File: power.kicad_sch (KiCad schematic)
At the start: 7 parts, among them J1 USB_C_Receptacle, U1 INA226, U2 AMS1117-3.3, U3 ATmega328P-A

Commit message: Getting there
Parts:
- added C3, C4: 22 pF, symbol Device:C
- added C5, C6: 1µF, symbol Device:C
- added R1, R2: 4.7kΩ, symbol Device:R
- added R3, R4: 5.1kΩ, symbol Device:R
- added Y1: Crystal, symbol Device:Crystal
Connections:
- net 3V3: now also C2.1, DS1.28 (VCC), U1.6 (VS), U1.8 (Vbus), U2.2 (VO), C6.2, R1.2, R2.1; no longer C2.2, DS1.9 (VDD)
- net GND: now also C2.2, C3.2, C4.2, C5.2, C6.1, R3.2, R4.2; no longer J1.S1 (SHIELD)
- net OLED_RESET: now reaches DS1.14 (~{RES})
- net OLED_RESET: now also U3.12 (PB0)
- net D/C: now reaches DS1.15 (D/~{C})
- net D/C: now also U3.13 (PB1)
- net R/W: now reaches DS1.16 (R/~{W})
- net R/W: now also U3.14 (PB2)
- net E/RD: now reaches DS1.17 (E/~{RD})
- net E/RD: now also U3.23 (PC0)
- net D0: now reaches DS1.18 (D0)
- net D0: now also U3.30 (PD0)
- net D1: now reaches DS1.19 (D1)
- net D1: now also U3.31 (PD1)
- net D2: now reaches DS1.20 (D2)
- net D2: now also U3.32 (PD2)
- net D3: now reaches DS1.21 (D3)
- net D3: now also U3.1 (PD3)
- net D4: now reaches DS1.22 (D4)
- net D4: now also U3.2 (PD4)
- net D5: now reaches DS1.23 (D5)
- net D5: now also U3.9 (PD5)
- net D6: now reaches DS1.24 (D6)
- net D6: now also U3.10 (PD6)
- net D7: now reaches DS1.25 (D7)
- net D7: now also U3.11 (PD7)
- net MOSI: now reaches U3.15 (PB3)
- net MISO: now reaches U3.16 (PB4)
- net SCK: now reaches U3.17 (PB5)
- net SDA: now reaches U3.27 (PC4)
- net SDA: now also U1.4 (SDA), R1.1
- net SCL: now reaches U3.28 (PC5)
- net SCL: now also U1.5 (SCL), R2.2
- net RESET: now reaches U3.29 (~{RESET}/PC6)
- net at U3.7 (XTAL1/PB6): now also C4.1, Y1.2
- net at U3.8 (XTAL2/PB7): now also C3.1, Y1.1
- net VBUS: now reaches C1.2, U2.3 (VI)
- net VBUS: now also J1.A4 (VBUS), J1.A9 (VBUS), J1.B4 (VBUS), J1.B9 (VBUS), U1.10 (Vin+)
- net at J1.A5 (CC1): now also R3.1
- net at J1.B5 (CC2): now also R4.1
- net INPUT_PW: now reaches U1.9 (Vin-)
- new net: C5.1, J1.S1 (SHIELD)
- no-connect marks 0 -> 5
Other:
- moved on the sheet: C2

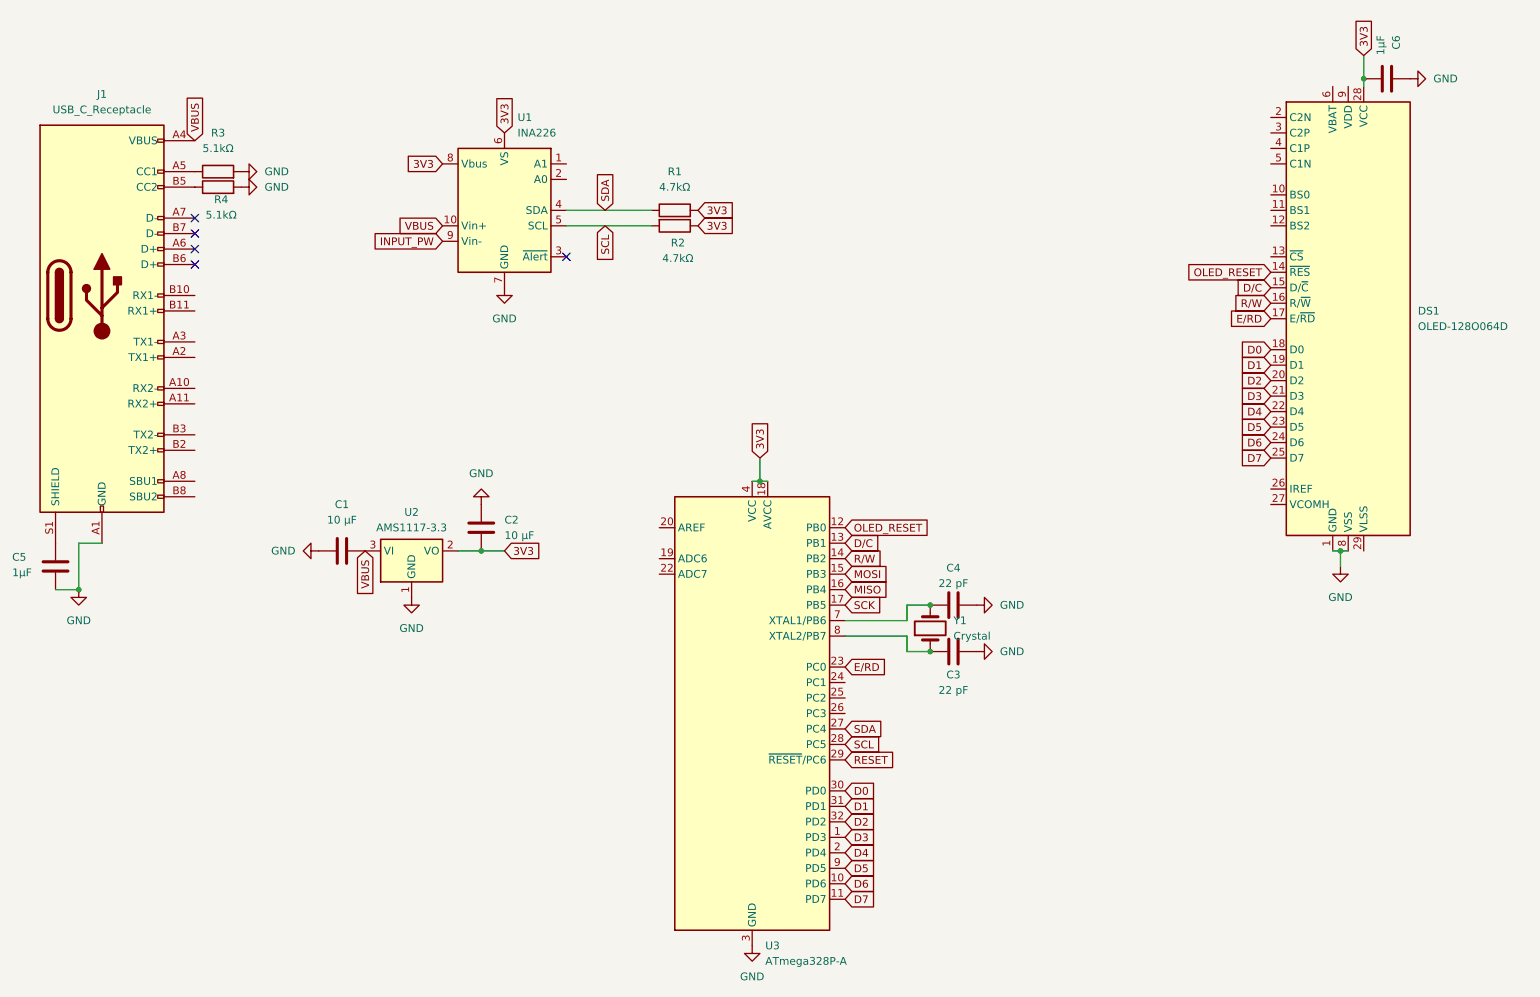
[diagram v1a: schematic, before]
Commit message: Added custom OLED, finished small changes to the schematic, and started the PCB
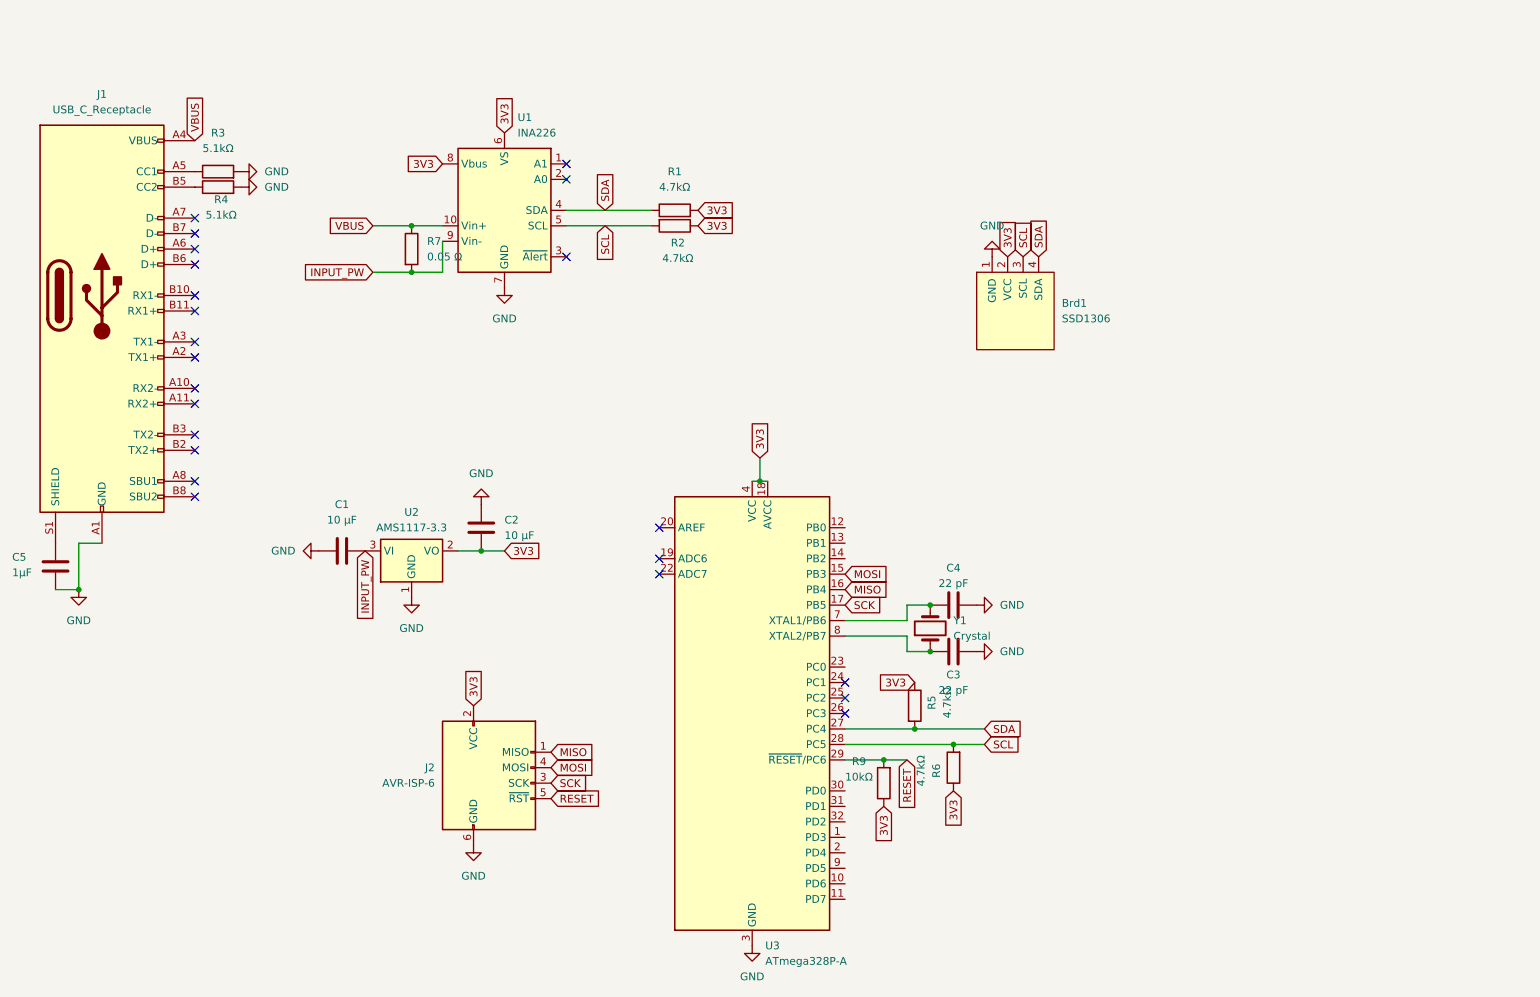
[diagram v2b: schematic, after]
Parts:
- removed C6: 1µF, symbol Device:C
- removed DS1: OLED-128O064D, Display:OLED-128O064D, symbol Display_Graphic:OLED-128O064D
- added Brd1: SSD1306, Display:Adafruit_SSD1306, symbol SSD1306:SSD1306
- added J2: AVR-ISP-6, Connector:Tag-Connect_TC2030-IDC-NL_2x03_P1.27mm_Vertical, symbol Connector:AVR-ISP-6
- added R5, R6: 4.7kΩ, Resistor_SMD:R_0603_1608Metric, symbol Device:R
- added R7: 0.05 Ω, Resistor_SMD:R_0603_1608Metric, symbol Device:R
- added R9: 10kΩ, Resistor_SMD:R_0603_1608Metric, symbol Device:R
- C1, C2, C3, C4, C5: footprint (none) -> Capacitor_SMD:C_0603_1608Metric
- J1: footprint (none) -> Connector_USB:USB_C_Receptacle_Amphenol_124019772112A
- R1, R2, R3, R4: footprint (none) -> Resistor_SMD:R_0603_1608Metric
- Y1: footprint (none) -> Crystal:Crystal_SMD_0603-2Pin_6.0x3.5mm
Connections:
- net 3V3: now also Brd1.2 (VCC), J2.2 (VCC), R5.1, R6.1, R9.1
- net GND: now also Brd1.1 (GND), J2.6 (GND)
- net INPUT_PW: now also C1.2, U2.3 (VI), R7.2
- net MISO: now also J2.1 (MISO)
- net MOSI: now also J2.4 (MOSI)
- net RESET: now also J2.5 (~{RST}), R9.2
- net SCK: now also J2.3 (SCK)
- net SCL: now also Brd1.3 (SCL), R6.2
- net SDA: now also Brd1.4 (SDA), R5.2
- net VBUS: now also R7.1; no longer C1.2, U2.3 (VI)
- net D0: no longer names the net of U3.30 (PD0)
- net D1: no longer names the net of U3.31 (PD1)
- net D2: no longer names the net of U3.32 (PD2)
- net D3: no longer names the net of U3.1 (PD3)
- net D4: no longer names the net of U3.2 (PD4)
- net D5: no longer names the net of U3.9 (PD5)
- net D6: no longer names the net of U3.10 (PD6)
- net D7: no longer names the net of U3.11 (PD7)
- net D/C: no longer names the net of U3.13 (PB1)
- net E/RD: no longer names the net of U3.23 (PC0)
- net OLED_RESET: no longer names the net of U3.12 (PB0)
- net R/W: no longer names the net of U3.14 (PB2)
- no-connect marks 5 -> 23

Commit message: PCB Routing Starting
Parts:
- added C6: 0.1 µF, symbol Device:C
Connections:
- net 3V3: now also C6.1
- net GND: now also C6.2
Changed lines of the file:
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@@
+	)
+	(junction
+		(at 182.88 45.72)
+		(diameter 0)
+		(color 0 0 0 0)
 	)
 	(junction
@@
 	(wire
 		(pts
+			(xy 182.88 40.64) (xy 182.88 45.72)
+		)
+		(stroke
+			(width 0)
+			(type default)
+		)
+	)
+	(wire
+		(pts
 			(xy 92.71 104.14) (xy 96.52 104.14)
 		)
@@
 	(wire
 		(pts
+			(xy 182.88 45.72) (xy 182.88 55.88)
+		)
+		(stroke
+			(width 0)
+			(type default)
+		)
+	)
+	(wire
+		(pts
 			(xy 167.64 133.35) (xy 156.21 133.35)
 		)
@@
 	(global_label "3V3"
 		(shape input)
-		(at 182.88 55.88 90)
+		(at 182.88 40.64 90)
 		(fields_autoplaced yes)
 		(effects
@@
 		)
 		(property "Intersheetrefs" "${INTERSHEET_REFS}"
-			(at 182.88 50.0414 90)
+			(at 182.88 34.8014 90)
 			(effects
 				(font
@@
 	)
 	(symbol
+		(lib_id "Device:C")
+		(at 186.69 45.72 90)
+		(unit 1)
+		(exclude_from_sim no)
+		(in_bom yes)
+		(on_board yes)
+		(dnp no)
+		(fields_autoplaced yes)
+		(property "Reference" "C6"
+			(at 186.69 38.1 90)
+			(effects
+				(font
+					(size 1.27 1.27)
+				)
+			)
+		)
+		(property "Value" "0.1 µF"
+			(at 186.69 40.64 90)
+			(effects
+				(font
+					(size 1.27 1.27)
+				)
+			)
+		)
+		(property "Footprint" ""
+			(at 190.5 44.7548 0)
+			(effects
+				(font
+					(size 1.27 1.27)
+				)
+				(hide yes)
+			)
+		)
+		(property "Datasheet" "~"
+			(at 186.69 45.72 0)
+			(effects
+				(font
+					(size 1.27 1.27)
+				)
+				(hide yes)
+			)
+		)
+		(property "Description" "Unpolarized capacitor"
+			(at 186.69 45.72 0)
+			(effects
+				(font
+					(size 1.27 1.27)
+				)
+				(hide yes)
+			)
+		)
+		(pin "2"
+		)
+		(pin "1"
+		)
+		(instances
+			(project ""
+				(path "/d55febbb-3d07-434c-b0dc-1571f6d3a46d"
+					(reference "C6")
+					(unit 1)
+				)
+			)
+		)
+	)
+	(symbol
 		(lib_id "power:GND")
 		(at 30.48 110.49 0)
@@
 					(unit 1)
 				)
+			)
+		)
+	)
+	(symbol
+		(lib_id "power:GND")
+		(at 190.5 45.72 90)
+		(unit 1)
+		(exclude_from_sim no)
+		(in_bom yes)
+		(on_board yes)
+		(dnp no)
+		(fields_autoplaced yes)
+		(property "Reference" "#PWR012"
+			(at 196.85 45.72 0)
+			(effects
+				(font
+					(size 1.27 1.27)
+				)
+				(hide yes)
+			)
+		)
+		(property "Value" "GND"
+			(at 194.31 45.7199 90)
+			(effects
+				(font
+					(size 1.27 1.27)
+				)
+				(justify right)
+			)
+		)
+		(property "Footprint" ""
+			(at 190.5 45.72 0)
+			(effects
+				(font
+					(size 1.27 1.27)
+				)
+				(hide yes)
+			)
+		)
+		(property "Datasheet" ""
+			(at 190.5 45.72 0)
+			(effects
+				(font
+					(size 1.27 1.27)
+				)
+				(hide yes)
+			)
+		)
+		(property "Description" "Power symbol creates a global label with name \"GND\" , ground"
+			(at 190.5 45.72 0)
+			(effects
+				(font
+					(size 1.27 1.27)
+				)
+				(hide yes)
+			)
+		)
+		(pin "1"
+		)
+		(instances
+			(project "power"
+				(path "/d55febbb-3d07-434c-b0dc-1571f6d3a46d"
+					(reference "#PWR012")
+					(unit 1)
+				)

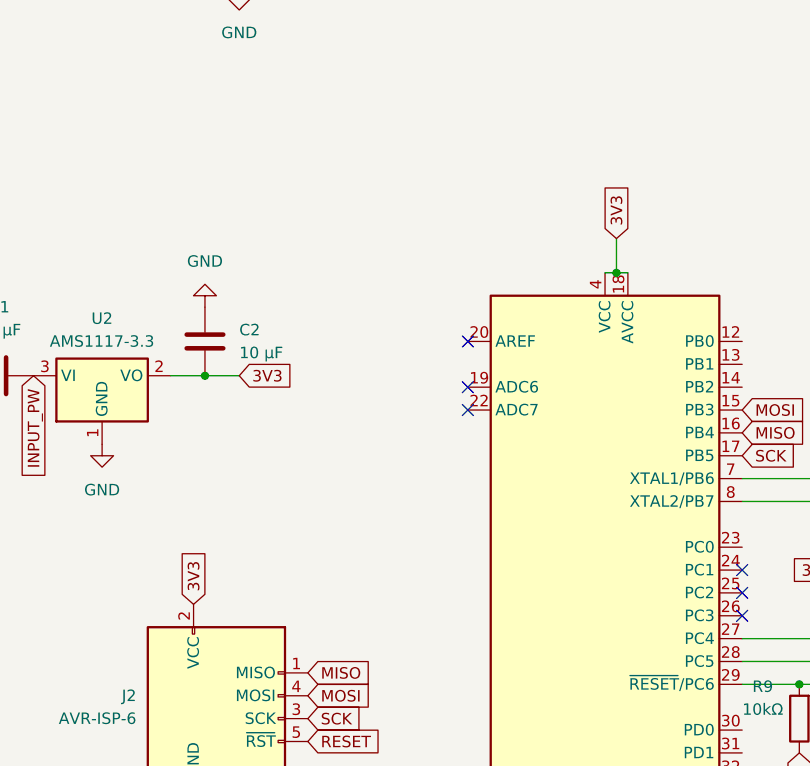
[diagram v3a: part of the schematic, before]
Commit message: Switched to 5V over 3.3V for MCU for programming
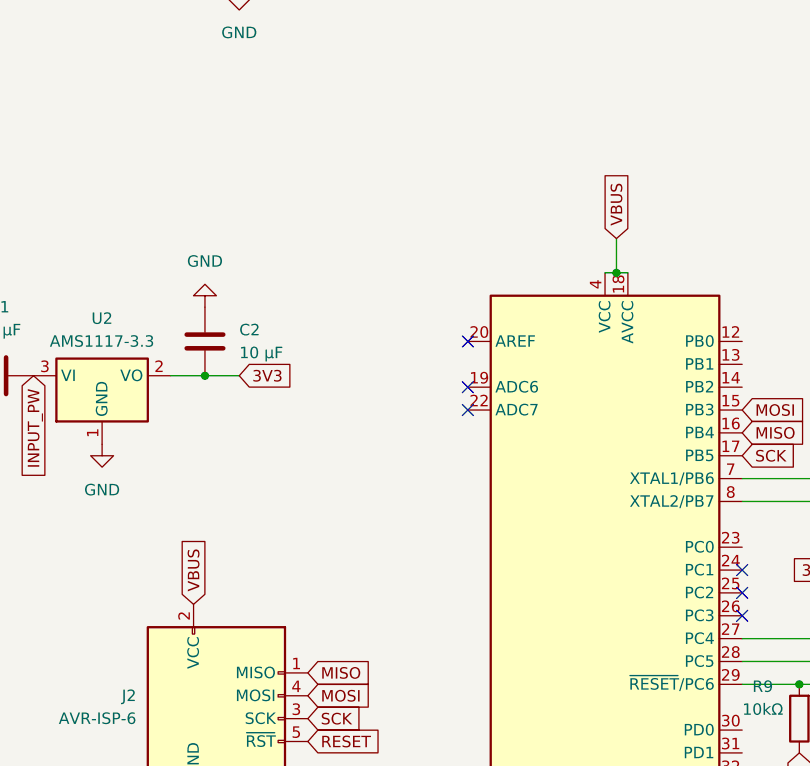
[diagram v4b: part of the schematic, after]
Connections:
- net 3V3: no longer J2.2 (VCC), U3.18 (AVCC), U3.4 (VCC), U3.6 (VCC)
- net VBUS: now also J2.2 (VCC), U3.18 (AVCC), U3.4 (VCC), U3.6 (VCC)
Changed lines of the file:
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@@
 		)
 	)
-	(global_label "3V3"
+	(global_label "VBUS"
 		(shape input)
 		(at 142.24 88.9 90)
@@
 		)
 		(property "Intersheetrefs" "${INTERSHEET_REFS}"
-			(at 142.24 83.0614 90)
+			(at 142.24 81.6704 90)
 			(effects
 				(font
@@
 		)
 	)
-	(global_label "3V3"
+	(global_label "VBUS"
 		(shape input)
 		(at 95.25 129.54 90)
@@
 		)
 		(property "Intersheetrefs" "${INTERSHEET_REFS}"
-			(at 95.25 123.7014 90)
-			(effects
-				(font
+			(at 95.25 122.3104 90)
+			(effects
+				(font

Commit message: Finished it all!
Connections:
- net GND: now also U1.1 (A1), U1.2 (A0)
- no-connect marks 23 -> 21
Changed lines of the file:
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@@
-	)
-	(no_connect
-		(at 110.49 40.64)
 	)
 	(no_connect
@@
 	(no_connect
 		(at 49.53 95.25)
-	)
-	(no_connect
-		(at 110.49 43.18)
 	)
 	(no_connect
@@
 	)
 	(symbol
+		(lib_id "power:GND")
+		(at 110.49 43.18 90)
+		(unit 1)
+		(exclude_from_sim no)
+		(in_bom yes)
+		(on_board yes)
+		(dnp no)
+		(fields_autoplaced yes)
+		(property "Reference" "#PWR015"
+			(at 116.84 43.18 0)
+			(effects
+				(font
+					(size 1.27 1.27)
+				)
+				(hide yes)
+			)
+		)
+		(property "Value" "GND"
+			(at 114.3 43.1799 90)
+			(effects
+				(font
+					(size 1.27 1.27)
+				)
+				(justify right)
+			)
+		)
+		(property "Footprint" ""
+			(at 110.49 43.18 0)
+			(effects
+				(font
+					(size 1.27 1.27)
+				)
+				(hide yes)
+			)
+		)
+		(property "Datasheet" ""
+			(at 110.49 43.18 0)
+			(effects
+				(font
+					(size 1.27 1.27)
+				)
+				(hide yes)
+			)
+		)
+		(property "Description" "Power symbol creates a global label with name \"GND\" , ground"
+			(at 110.49 43.18 0)
+			(effects
+				(font
+					(size 1.27 1.27)
+				)
+				(hide yes)
+			)
+		)
+		(pin "1"
+		)
+		(instances
+			(project "power"
+				(path "/d55febbb-3d07-434c-b0dc-1571f6d3a46d"
+					(reference "#PWR015")
+					(unit 1)
+				)
+			)
+		)
+	)
+	(symbol
 		(lib_id "MCU_Microchip_ATmega:ATmega328P-A")
 		(at 140.97 130.81 0)
@@
 					(unit 1)
 				)
+			)
+		)
+	)
+	(symbol
+		(lib_id "power:GND")
+		(at 110.49 40.64 90)
+		(unit 1)
+		(exclude_from_sim no)
+		(in_bom yes)
+		(on_board yes)
+		(dnp no)
+		(fields_autoplaced yes)
+		(property "Reference" "#PWR013"
+			(at 116.84 40.64 0)
+			(effects
+				(font
+					(size 1.27 1.27)
+				)
+				(hide yes)
+			)
+		)
+		(property "Value" "GND"
+			(at 114.3 40.6399 90)
+			(effects
+				(font
+					(size 1.27 1.27)
+				)
+				(justify right)
+			)
+		)
+		(property "Footprint" ""
+			(at 110.49 40.64 0)
+			(effects
+				(font
+					(size 1.27 1.27)
+				)
+				(hide yes)
+			)
+		)
+		(property "Datasheet" ""
+			(at 110.49 40.64 0)
+			(effects
+				(font
+					(size 1.27 1.27)
+				)
+				(hide yes)
+			)
+		)
+		(property "Description" "Power symbol creates a global label with name \"GND\" , ground"
+			(at 110.49 40.64 0)
+			(effects
+				(font
+					(size 1.27 1.27)
+				)
+				(hide yes)
+			)
+		)
+		(pin "1"
+		)
+		(instances
+			(project "power"
+				(path "/d55febbb-3d07-434c-b0dc-1571f6d3a46d"
+					(reference "#PWR013")
+					(unit 1)
+				)

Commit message: Possibly fixed it
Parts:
- added J3: Screw_Terminal_01x02, TerminalBlock_4Ucon:TerminalBlock_4Ucon_1x02_P3.50mm_Horizontal, symbol Connector:Screw_Terminal_01x02
- C6: footprint (none) -> Capacitor_SMD:C_0603_1608Metric
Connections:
- net INPUT_PW is gone; now on net VBUS: C1.2, R7.2, U1.9 (Vin-), U2.3 (VI)
- net GND: now also J3.2 (Pin_2); no longer R3.2, R4.2
- net VBUS: no longer J2.2 (VCC), R7.1, U1.10 (Vin+), U3.18 (AVCC), U3.4 (VCC), U3.6 (VCC)
- new net +5V: J2.2 (VCC), J3.1 (Pin_1), R3.2, R4.2, R7.1, U1.10 (Vin+), U3.18 (AVCC), U3.4 (VCC), U3.6 (VCC)
